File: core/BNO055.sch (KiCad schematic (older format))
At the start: 9 parts, among them U4 BNO055

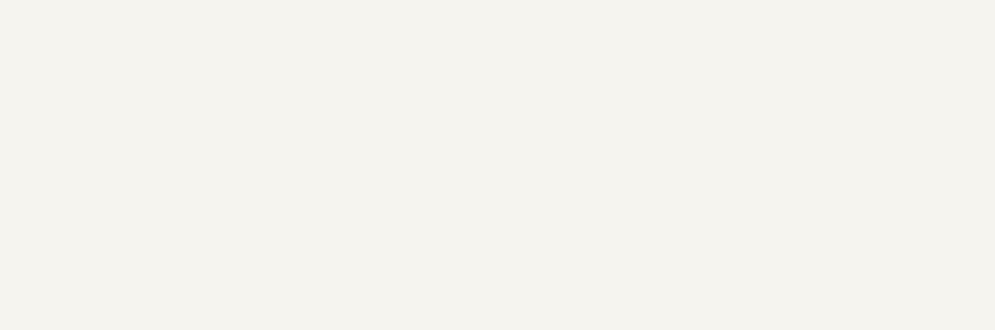
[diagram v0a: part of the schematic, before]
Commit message: Updated core with IMU hierarchical block
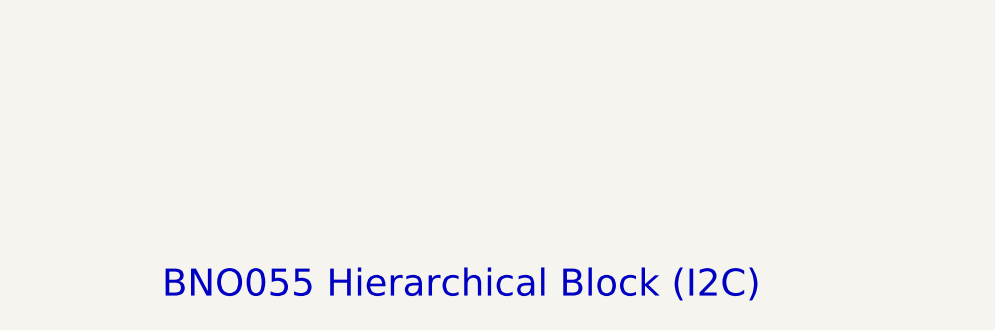
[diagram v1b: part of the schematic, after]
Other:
- note added: "BNO055 Hierarchical Block (I2C)"
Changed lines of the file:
@@
 SCL
 Connection ~ 5200 4200
+Text Notes 7300 6900 0    118  ~ 0
+BNO055 Hierarchical Block (I2C)
 $EndSCHEMATC
